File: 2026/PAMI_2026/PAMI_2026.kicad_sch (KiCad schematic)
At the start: 59 parts, among them IC1 Transfo 5V -> 3.3V, J1 USB-C_12pin, J10 RANGE, J11 RANGE, J12 22-03-5035, J13 Conn_01x02_Pin, J14 Conn_01x02_Pin, J15 Conn_01x02_Pin, J2 Screw_Terminal_01x02, J3 Stepper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

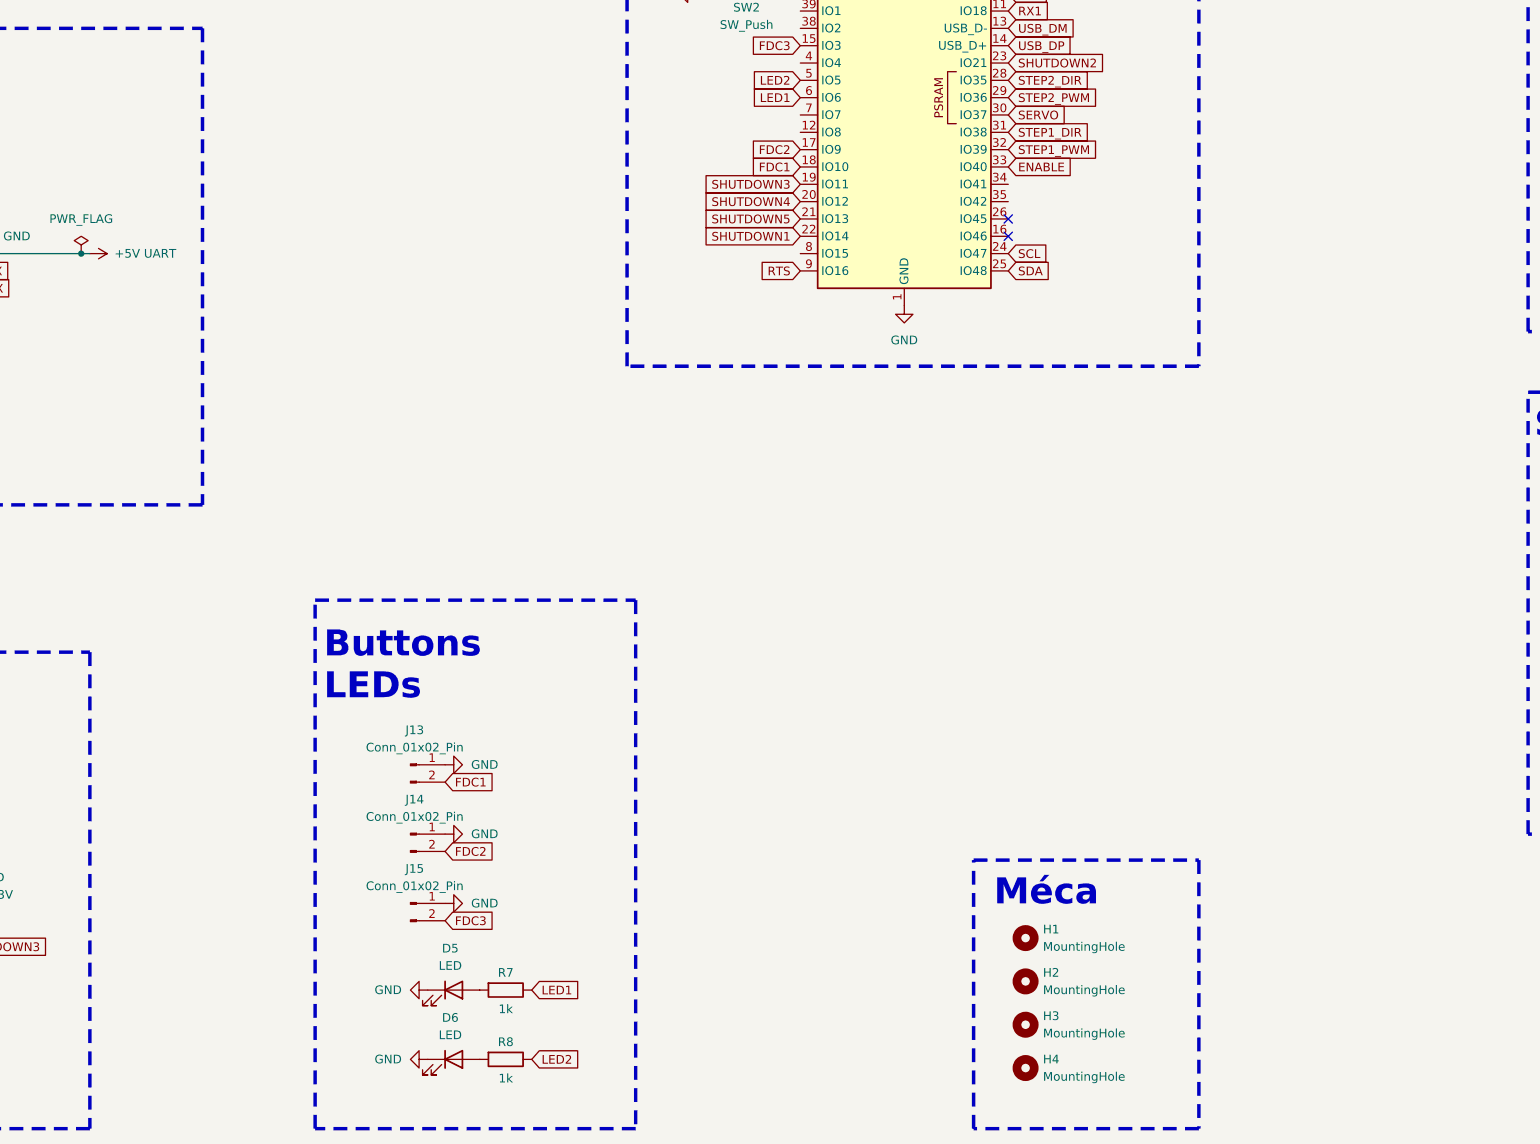
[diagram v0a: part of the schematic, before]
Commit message: [PAMI 2026] Add IMU.
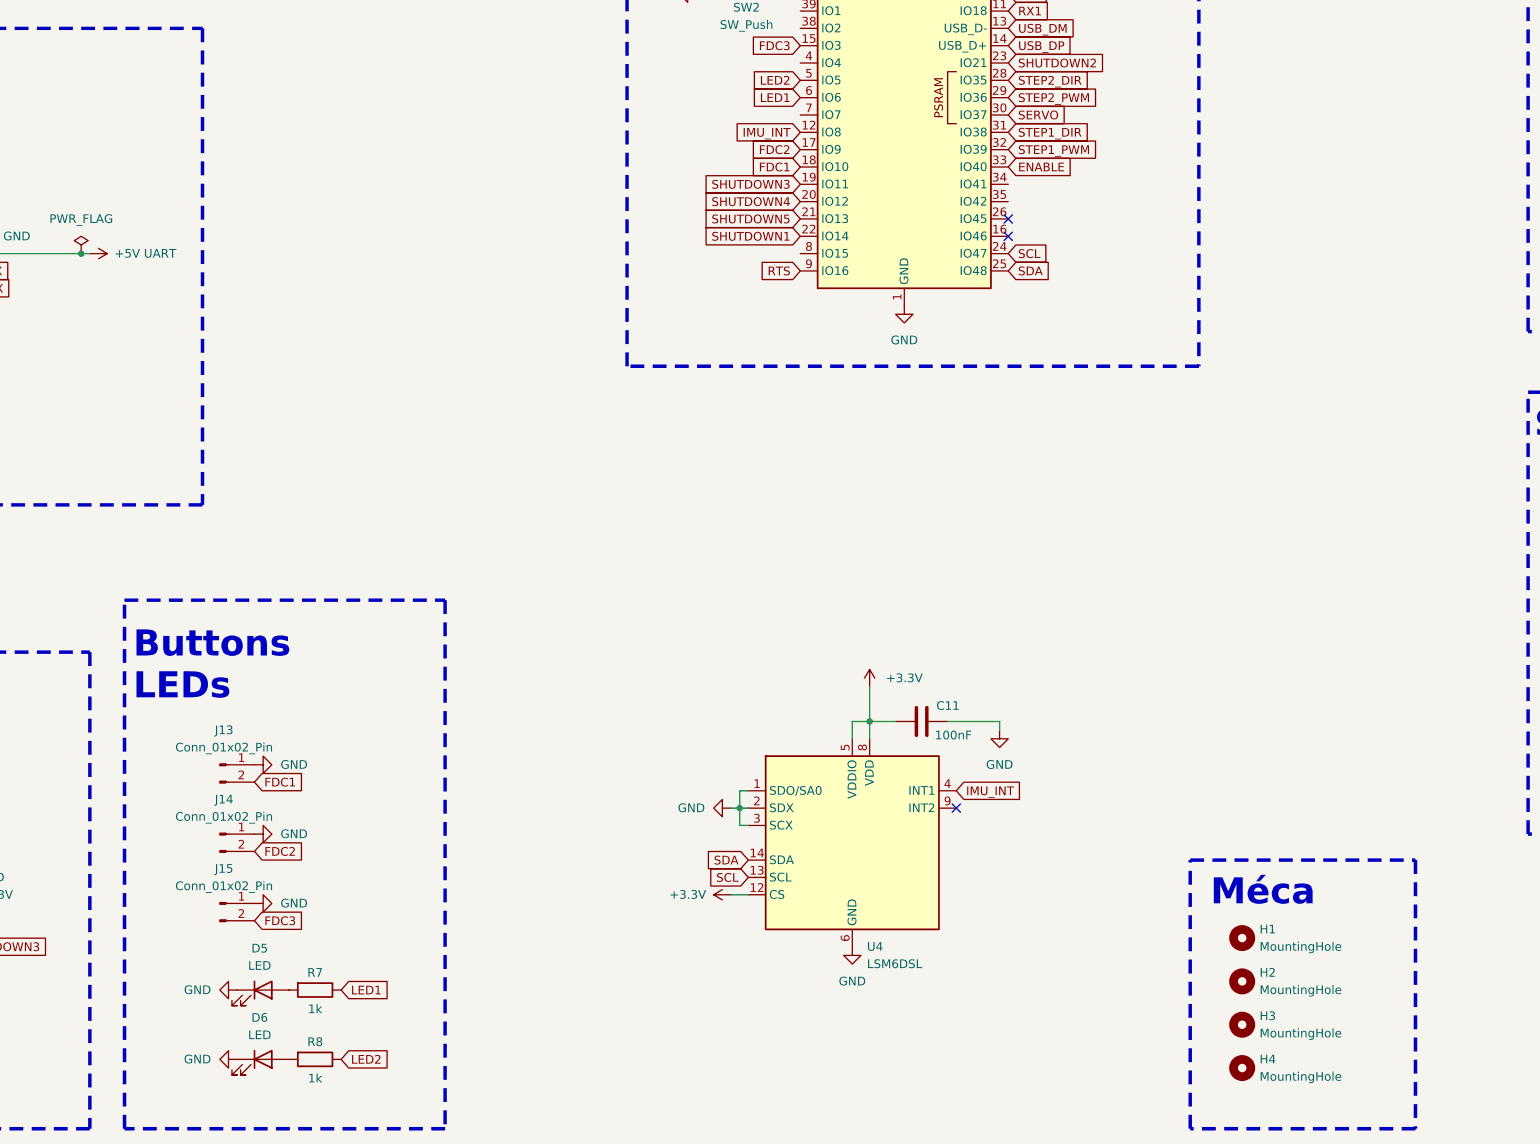
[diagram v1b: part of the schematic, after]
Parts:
- added C11: 100nF, Capacitor_SMD:C_0603_1608Metric, symbol Device:C
- added U4: LSM6DSL, Package_LGA:LGA-14_3x2.5mm_P0.5mm_LayoutBorder3x4y, symbol Sensor_Motion:LSM6DSL
- C10: footprint Capacitor_SMD:C_0805_2012Metric -> Capacitor_SMD:C_0603_1608Metric
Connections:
- net +3.3V: now also C11.1, U4.12 (CS), U4.5 (VDDIO), U4.8 (VDD)
- net GND: now also C11.2, U4.1 (SDO/SA0), U4.2 (SDX), U4.3 (SCX), U4.6 (GND), U4.7 (GND)
- net SCL: now also U4.13 (SCL)
- net SDA: now also U4.14 (SDA)
- net IMU_INT: now reaches U1.12 (IO8)
- net IMU_INT: now also U4.4 (INT1)
- no-connect marks 4 -> 5
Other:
- moved on the sheet: D5, D6, H1, H2, H3, H4, J13, J14, J15, R7, R8
